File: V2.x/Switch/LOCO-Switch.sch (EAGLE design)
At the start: 55 parts, among them IC1 Atmega 328-P, IC2 MCP2515, IC3 ACS712ELCTR-20A-T, IC5 LM340MP-05, J1 3-794618-4, J2 3-794618-4, Q1 8MHz, Q2 16MHz, Q3 FDS5680, Q4 FDS5680, Q5 FDS5680, Q6 FDS5680, Q7 FDS5680, Q8 FDS5680, X1 22-23-2081

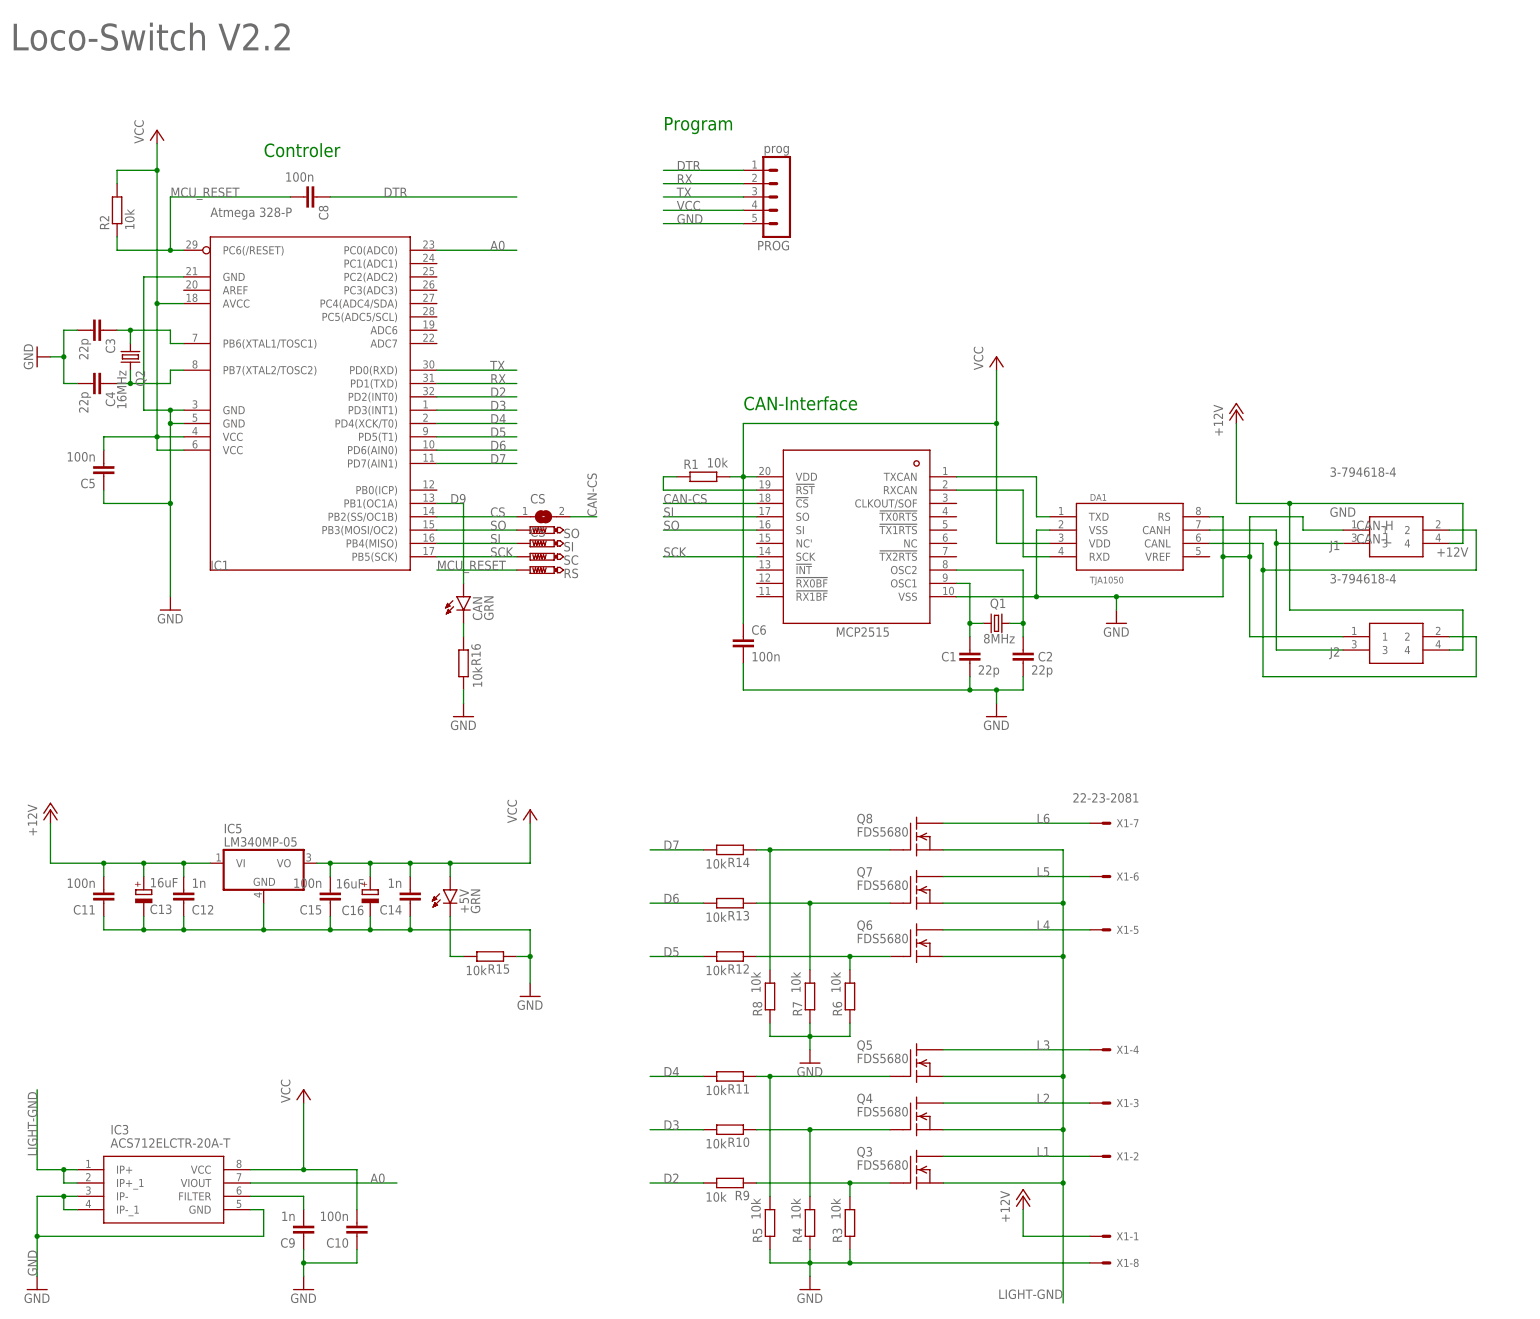
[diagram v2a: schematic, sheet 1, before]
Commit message: changed sch and brd of motor and switch for RX/TX leds
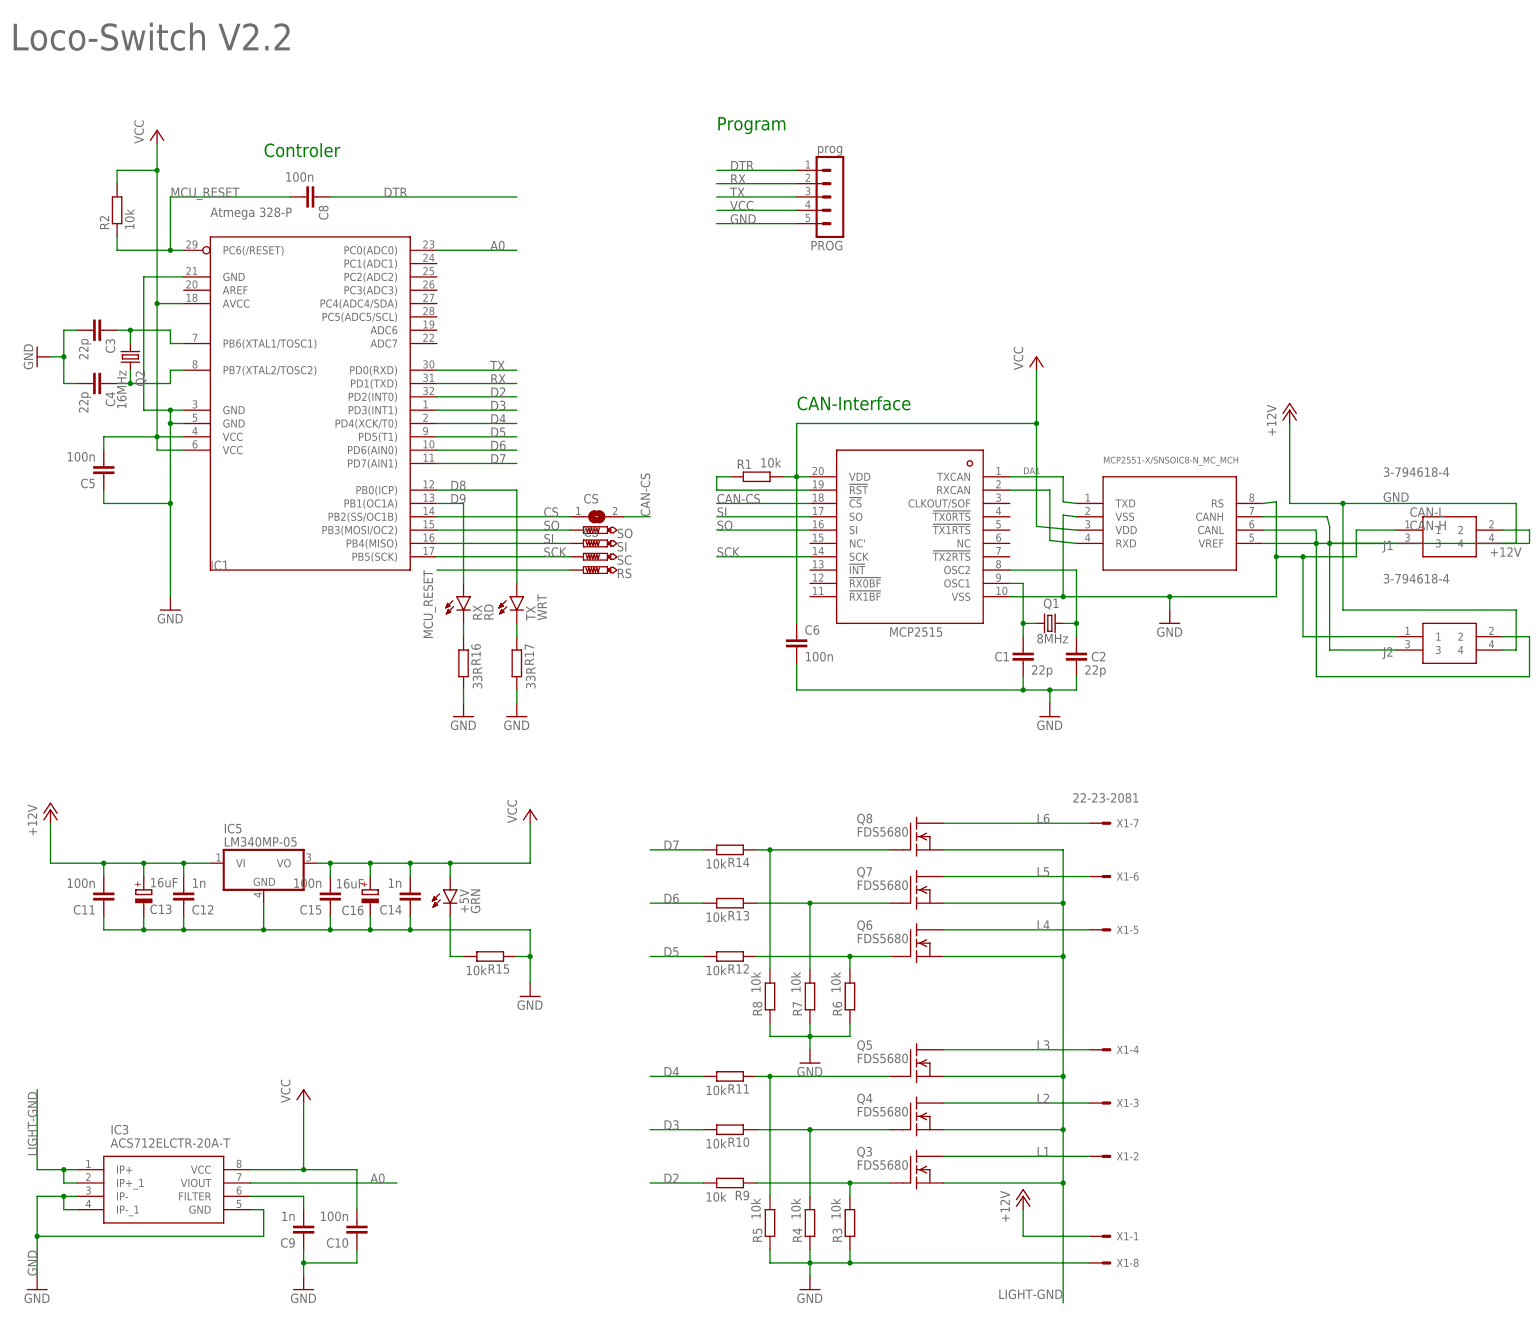
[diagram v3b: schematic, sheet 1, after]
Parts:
- added R17: 33R, rcl:R-EU_R0603
- added TX: WRT, led:LEDCHIP-LED0603
- DA1: value TJA1050 -> MCP2551-X/SNSOIC8-N_MC_MCH; device TJA1050:TJA1050 -> MCP2551:MCP2551-X/SNSOIC8-N_MC_MCH
- IC1: device atmel:MEGA8-AI -> atmel:MEGA8
- IC2: device mcp2514:MCP2515 -> MCP2515:MCP2515
- J1, J2: device SamacSys_Parts:3-794618-4 -> Micro Mate-N-Lok:3-794618-4
- PROG: device con-lstb:MA05-1 -> lst-b:MA05-1
- R16: value 10k -> 33R
- RX: value GRN -> RD
- renumbered CAN to RX
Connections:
- new net D8: IC1.PB0(ICP), TX.A
- new net N$13: R17.1, TX.C
- net CAN-L: now also DA1.VREF
- net GND: now also R17.2
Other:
- moved on the sheet: C1, C2, C6, CS, J1, J2, PROG, Q1, R1, RS, SC, SI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
